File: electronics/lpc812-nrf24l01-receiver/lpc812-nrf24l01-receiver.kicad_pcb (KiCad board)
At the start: 2 copper layers, 25 x 29 mm, 21 parts, among them K1 BAT, K2 CH3, K3 TH, K4 ST, P1 NRF24L01+, SW1 ISP/BIND, U1 MCP1703, U2 LPC812, X1 16 MHz

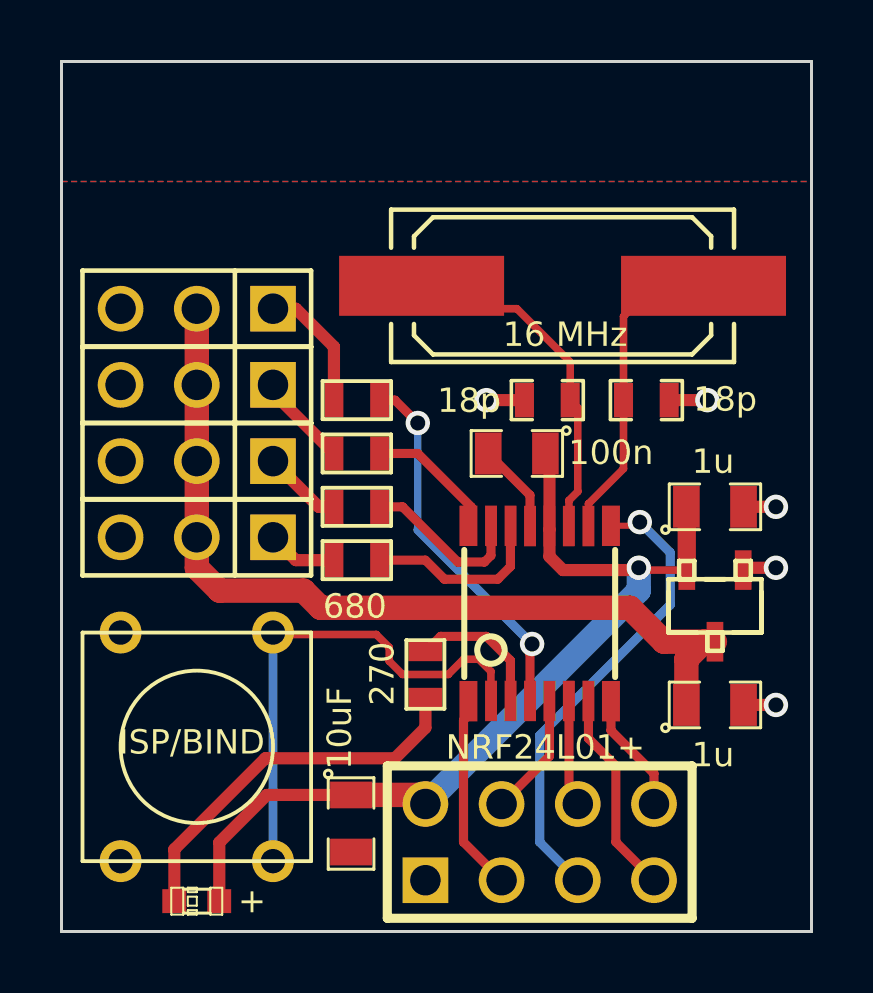
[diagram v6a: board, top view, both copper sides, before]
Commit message: Re-layout the board with different servo connector positions
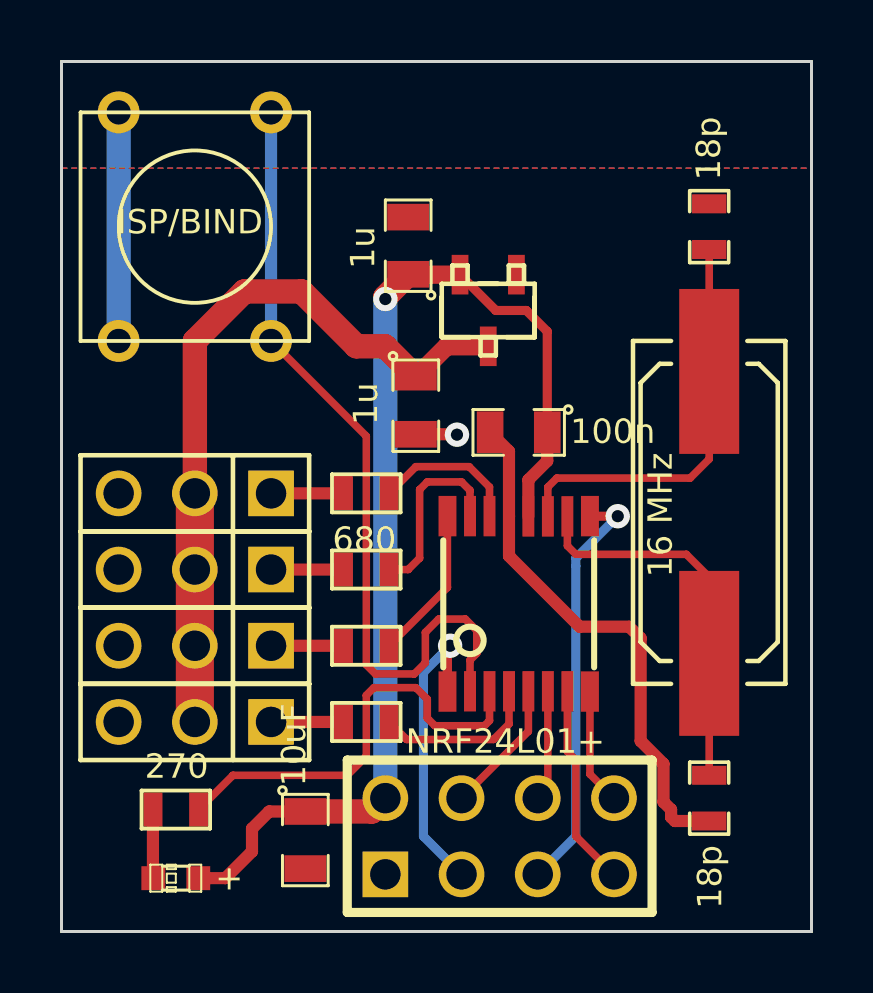
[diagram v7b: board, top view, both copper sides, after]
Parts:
- moved SW1 17.3 mm to (67.4, 62.5)
- moved C2 14.1 mm to (74.8, 68.5), turned to 270 degrees
- moved K1 13.8 mm to (67.4, 79.0)
- moved C4 13.4 mm to (84.6, 81.6), turned to 270 degrees
- moved C3 13.4 mm to (74.6, 63.1), turned to 90 degrees
- moved U1 12.4 mm to (77.2, 65.3)
- moved R2 10.7 mm to (73.2, 79.0)
- moved R1 9.46 mm to (66.8, 81.9), turned to 0 degrees
- moved X1 9.00 mm to (84.6, 72.0), turned to 90 degrees
- moved K2 8.70 mm to (67.4, 76.5)
- moved C5 7.91 mm to (84.6, 62.5), turned to 90 degrees
- moved R3 6.42 mm to (73.2, 76.5)
- moved K3 3.62 mm to (67.4, 73.9)
- moved R5 2.25 mm to (73.2, 71.4)
- moved R4 2.11 mm to (73.2, 73.9)
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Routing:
- net VSS: track 8.95 -> 26.6 mm, vias 5 -> 1
- net N-000007: track 12.8 -> 2.29 mm
- net /ISP-BIND: track 17.2 -> 27.2 mm
- net /LED: track 4.66 -> 14.5 mm
- net /Tx: track 12.7 -> 5.54 mm, vias 2 -> 0
- net +3.3V: track 30.8 -> 37.4 mm
- net +BATT: track 29.3 -> 24.8 mm
- net /CE: track 6.73 -> 10.1 mm, vias 0 -> 1
- net /XTALOUT: track 10.8 -> 12.7 mm
- net N-0000012: track 4.34 -> 2.41 mm
- net /XTALIN: track 11.9 -> 13.7 mm
- net /SCK: track 15.7 -> 14.0 mm
- net /CH1: track 6.03 -> 4.96 mm
- net /CH2: track 5.43 -> 6.22 mm
- net N-0000011: track 3.13 -> 2.41 mm
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
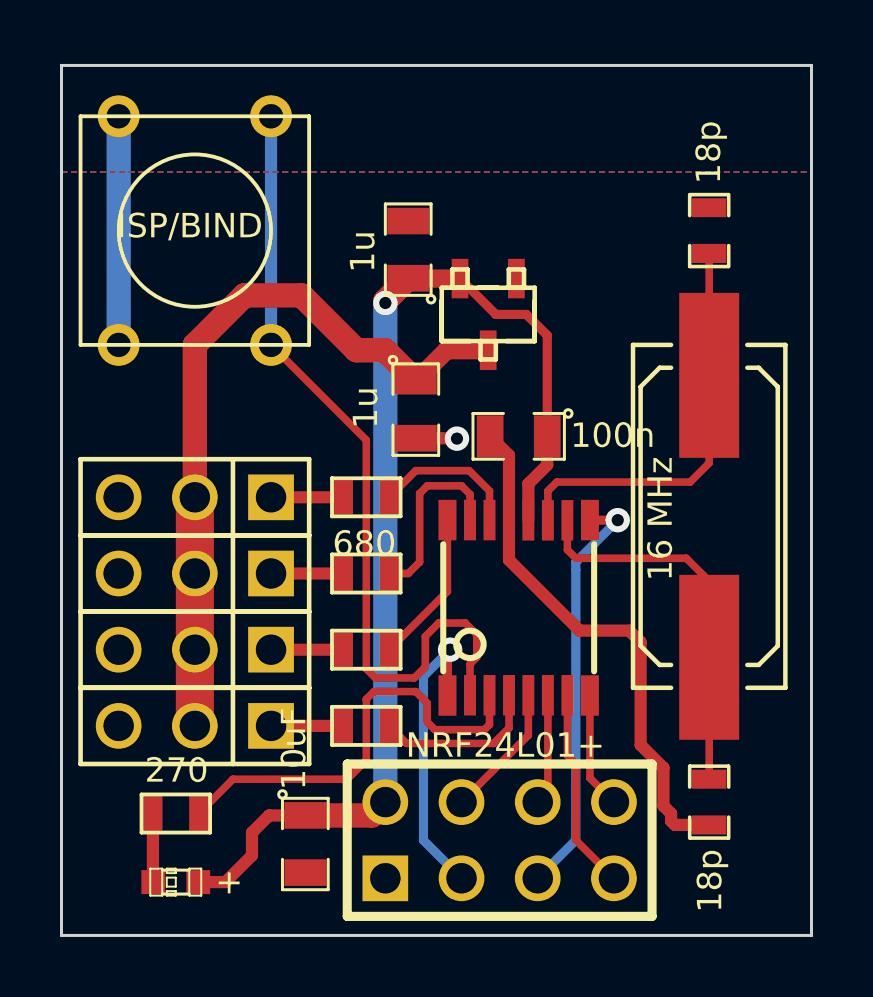
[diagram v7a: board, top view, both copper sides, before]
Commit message: Tweak board for least amount of vias; Add more silk screen
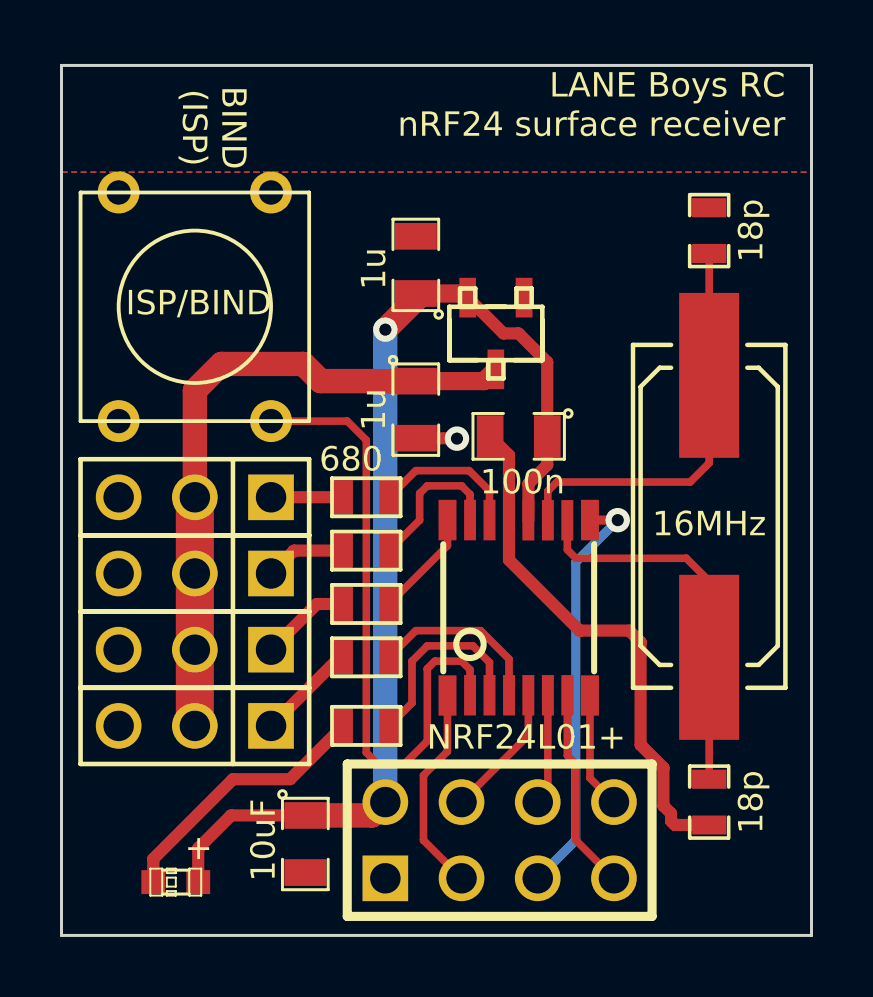
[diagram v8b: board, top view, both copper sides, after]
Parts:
- X1: value 16 MHz -> 16MHz
- moved R1 6.99 mm to (73.2, 79.0)
- moved SW1 2.54 mm to (67.4, 65.0)
- moved R2 2.29 mm to (73.2, 76.7)
- moved R3 1.52 mm to (73.2, 75.0)
- moved R4 0.76 mm to (73.2, 73.2)
- moved U1 0.68 mm to (77.5, 65.9)
- moved C3 0.57 mm to (74.8, 63.6)
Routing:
- net /LED: track 14.5 -> 6.59 mm
- net VSS: track 26.6 -> 19.0 mm
- net N-000007: track 2.29 -> 8.95 mm
- net /ISP-BIND: track 27.2 -> 21.3 mm
- net /CE: track 10.1 -> 6.95 mm, vias 1 -> 0
- net +BATT: track 24.8 -> 22.0 mm
- net /CH3-Rx: track 5.13 -> 3.60 mm
- net +3.3V: track 37.4 -> 36.2 mm
- net /CH2: track 6.22 -> 5.09 mm
- net N-0000012: track 2.41 -> 3.36 mm
- net N-0000011: track 2.41 -> 3.04 mm
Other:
- board text added: "(Rx)"
- board text added: "(Tx)"
- board text added: "BAT"
- board text added: "BIND (ISP)"
- board text added: "CH3"
- board text added: "LANE Boys RC nRF24 surface receiver"
- board text added: "Rev 1"
- board text added: "ST"
- board text added: "TH"
